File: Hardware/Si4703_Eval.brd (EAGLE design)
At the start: 22.9 x 31.8 mm, 37 parts, among them U1 SI4703, U3 TPA6111, Y1 32.768kHz

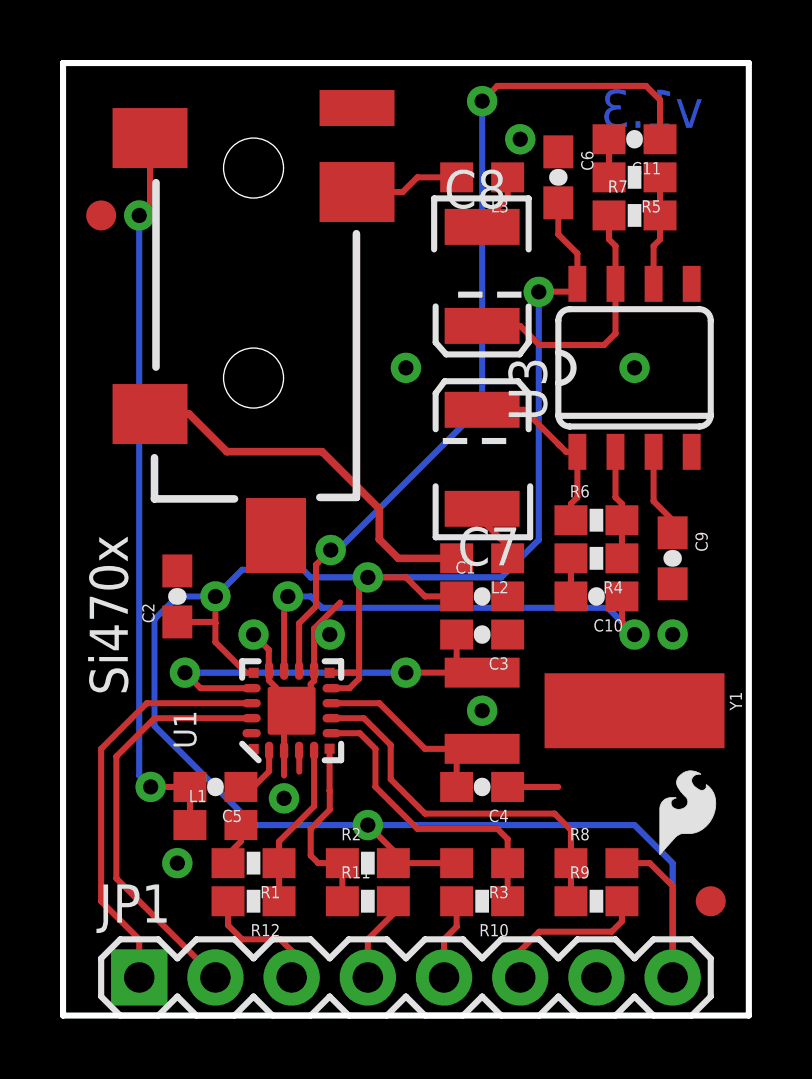
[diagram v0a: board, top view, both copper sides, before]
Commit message: fixing I2C breakout order, adding board name to file
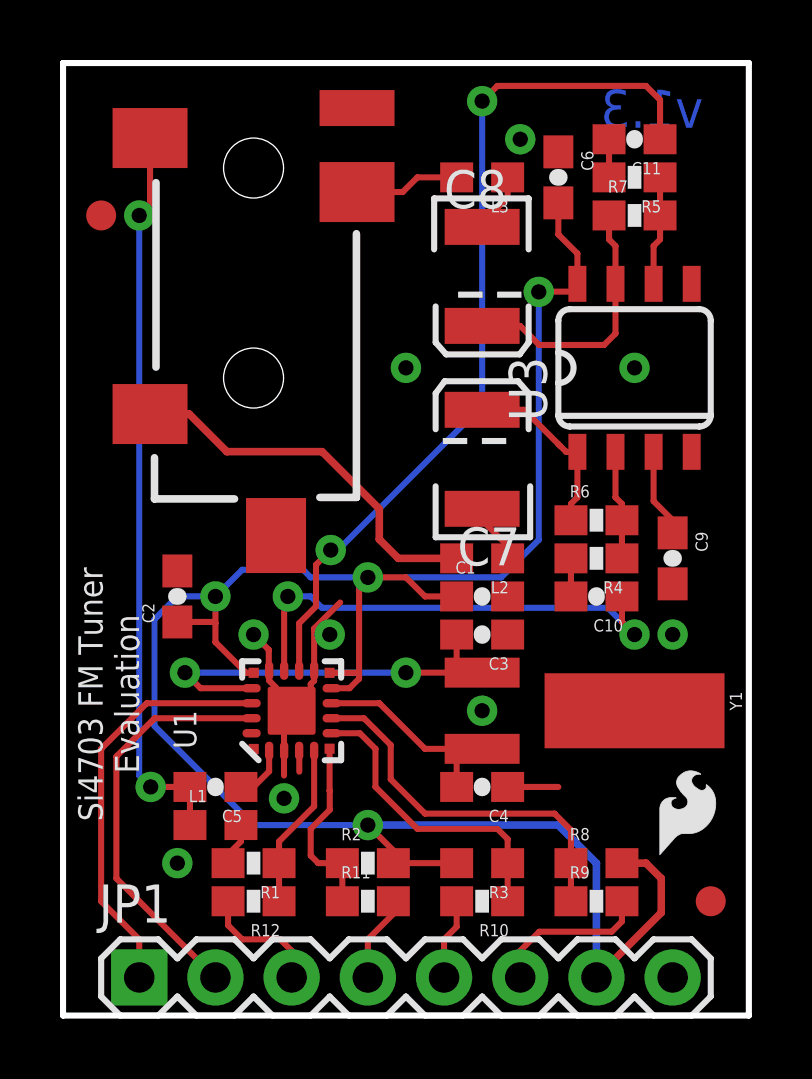
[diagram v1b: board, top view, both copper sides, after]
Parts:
- added U$1: REVISION, SparkFun-Aesthetics:REVISION
- moved FRAME2 31.8 mm to (-12.7, -8.89)
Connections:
- net 3.3V: now also JP1.7; no longer JP1.8
- net GND: now also JP1.8; no longer JP1.7
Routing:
- net 3.3V: track 75.4 -> 73.6 mm
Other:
- board text added: "N. Seidle"
- board text added: "Si4703 FM Tuner Evaluation"
- board text removed: "Si470x"
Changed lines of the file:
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@@
 <layer number="18" name="Vias" color="2" fill="1" visible="yes" active="yes"/>
 <layer number="19" name="Unrouted" color="6" fill="1" visible="yes" active="yes"/>
-<layer number="20" name="Dimension" color="6" fill="1" visible="yes" active="yes"/>
+<layer number="20" name="Dimension" color="15" fill="1" visible="yes" active="yes"/>
 <layer number="21" name="tPlace" color="16" fill="1" visible="yes" active="yes"/>
-<layer number="22" name="bPlace" color="14" fill="1" visible="no" active="yes"/>
+<layer number="22" name="bPlace" color="14" fill="1" visible="yes" active="yes"/>
 <layer number="23" name="tOrigins" color="15" fill="1" visible="yes" active="yes"/>
 <layer number="24" name="bOrigins" color="15" fill="1" visible="yes" active="yes"/>
@@
 <layer number="47" name="Measures" color="7" fill="1" visible="no" active="yes"/>
 <layer number="48" name="Document" color="7" fill="1" visible="no" active="yes"/>
-<layer number="49" name="Reference" color="7" fill="1" visible="no" active="yes"/>
+<layer number="49" name="Reference" color="7" fill="1" visible="yes" active="yes"/>
 <layer number="50" name="dxf" color="7" fill="1" visible="no" active="yes"/>
 <layer number="51" name="tDocu" color="6" fill="1" visible="yes" active="yes"/>
@@
 <layer number="106" name="bPlate" color="7" fill="1" visible="no" active="yes"/>
 <layer number="107" name="Crop" color="7" fill="1" visible="no" active="yes"/>
-<layer number="108" name="tplace-old" color="10" fill="1" visible="yes" active="yes"/>
-<layer number="109" name="ref-old" color="11" fill="1" visible="yes" active="yes"/>
+<layer number="108" name="tplace-old" color="10" fill="1" visible="no" active="yes"/>
+<layer number="109" name="ref-old" color="11" fill="1" visible="no" active="yes"/>
 <layer number="116" name="Patch_BOT" color="9" fill="4" visible="no" active="yes"/>
 <layer number="121" name="_tsilk" color="7" fill="1" visible="no" active="yes"/>
@@
 <text x="4.445" y="2.667" size="1.27" layer="22" font="vector" ratio="15" rot="MR90">GPIO1</text>
 <text x="1.905" y="2.667" size="1.27" layer="22" font="vector" ratio="15" rot="MR90">GPIO2</text>
-<text x="2.159" y="10.668" size="1.27" layer="21" font="vector" ratio="15" rot="R90">Si470x</text>
+<text x="2.54" y="6.477" size="0.8128" layer="21" font="vector" ratio="15" rot="R90">Si4703 FM Tuner
+     Evaluation</text>
 <text x="21.336" y="29.591" size="1.27" layer="16" font="vector" ratio="20" rot="SMR0">v1.3</text>
+<text x="17.78" y="-8.89" size="1.778" layer="51" font="vector" ratio="15">N. Seidle</text>
 </plain>
 <attributes>
@@
 <element name="JP5" library="SparkFun" package="FIDUCIAL-1X2" value="FIDUCIAL1X2" x="1.27" y="26.67"/>
 <element name="U4" library="SparkFun-Connectors" package="AUDIO-JACK-3.5MM-SMD" value="" x="6.35" y="31.75" rot="R270"/>
-<element name="FRAME2" library="SparkFun-Aesthetics" package="CREATIVE_COMMONS" value="FRAME-LETTER" x="17.78" y="-17.78"/>
+<element name="FRAME2" library="SparkFun-Aesthetics" package="CREATIVE_COMMONS" value="FRAME-LETTER" x="-12.7" y="-8.89"/>
 <element name="LOGO1" library="SparkFun-Aesthetics" package="SFE_LOGO_NAME_FLAME_.1" value="SFE_LOGO_NAME_FLAME.1_INCH" x="17.272" y="15.494" rot="MR0"/>
 <element name="LOGO2" library="SparkFun-Aesthetics" package="OSHW-LOGO-S" value="OSHW-LOGOS" x="19.431" y="27.051" rot="MR0"/>
+<element name="U$1" library="SparkFun-Aesthetics" package="REVISION" value="REVISION" x="-33.02" y="-12.7"/>
 </elements>
 <signals>
@@
 <contactref element="C6" pad="1"/>
 <contactref element="R1" pad="2"/>
-<contactref element="JP1" pad="7"/>
 <wire x1="8.37" y1="11.495" x2="8.37" y2="12.9013" width="0.2032" layer="1"/>
 <wire x1="8.37" y1="12.9013" x2="9.238" y2="13.7693" width="0.2032" layer="1"/>
@@
 <wire x1="6.87" y1="11.495" x2="6.87" y2="11.442" width="0.2032" layer="1"/>
 <wire x1="6.87" y1="11.442" x2="6.858" y2="11.43" width="0.2032" layer="1"/>
+<contactref element="JP1" pad="8"/>
 </signal>
 <signal name="N$1">
@@
 <contactref element="C1" pad="1"/>
 <contactref element="C6" pad="2"/>
-<contactref element="JP1" pad="8"/>
 <contactref element="U3" pad="8"/>
 <wire x1="6.355" y1="11.425" x2="6.35" y2="11.43" width="0.2032" layer="1"/>
 <wire x1="11.01" y1="5.08" x2="13.12" y2="5.08" width="0.2032" layer="1"/>
-<wire x1="20.32" y1="5.08" x2="20.32" y2="1.27" width="0.2032" layer="16"/>
-<wire x1="19.05" y1="6.35" x2="20.32" y2="5.08" width="0.2032" layer="16"/>
-<wire x1="10.16" y1="6.35" x2="19.05" y2="6.35" width="0.2032" layer="16"/>
 <wire x1="6.35" y1="6.35" x2="10.16" y2="6.35" width="0.2032" layer="16"/>
 <wire x1="3.048" y1="9.652" x2="6.35" y2="6.35" width="0.2032" layer="16"/>
@@
 <via x="5.08" y="13.97" extent="1-16" drill="0.508"/>
 <via x="10.16" y="6.35" extent="1-16" drill="0.508"/>
-<wire x1="18.63" y1="5.08" x2="19.558" y2="5.08" width="0.2032" layer="1"/>
-<wire x1="19.558" y1="5.08" x2="20.32" y2="4.318" width="0.2032" layer="1"/>
-<wire x1="20.32" y1="4.318" x2="20.32" y2="1.27" width="0.2032" layer="1"/>
 <wire x1="17.0688" y1="24.13" x2="15.8648" y2="24.13" width="0.2032" layer="1"/>
 <wire x1="15.8648" y1="24.13" x2="15.8572" y2="24.1224" width="0.2032" layer="1"/>
@@
 <wire x1="17.0688" y1="24.13" x2="17.0688" y2="24.3138" width="0.2032" layer="1"/>
 <wire x1="17.0688" y1="24.3138" x2="17.145" y2="24.39" width="0.2032" layer="1"/>
+<contactref element="JP1" pad="7"/>
+<wire x1="10.16" y1="6.35" x2="16.51" y2="6.35" width="0.254" layer="16"/>
+<wire x1="16.51" y1="6.35" x2="17.78" y2="5.08" width="0.254" layer="16"/>
+<wire x1="17.78" y1="5.08" x2="17.78" y2="1.27" width="0.254" layer="16"/>
+<wire x1="18.63" y1="5.08" x2="19.431" y2="5.08" width="0.254" layer="1"/>
+<wire x1="19.431" y1="5.08" x2="19.939" y2="4.572" width="0.254" layer="1"/>
+<wire x1="19.939" y1="4.572" x2="19.939" y2="3.429" width="0.254" layer="1"/>
+<wire x1="19.939" y1="3.429" x2="17.78" y2="1.27" width="0.254" layer="1"/>
 </signal>
 <signal name="N$4">
@@
 </board>
 </drawing>
+<compatibility>
+<note version="6.3" minversion="6.2.2" severity="warning">
+Since Version 6.2.2 text objects can contain more than one line,
+which will not be processed correctly with this version.
+</note>
+</compatibility>
 </eagle>
